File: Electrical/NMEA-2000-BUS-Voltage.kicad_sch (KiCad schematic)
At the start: 68 parts, among them IC1 ADS131M08QPBSRQ1, J1 DE9_Receptacle, J2 Conn_01x04, J3 Conn_01x02, J4 Conn_01x04, J5 Conn_01x05, J6 Conn_01x02, Q1 IRFZ44N, SW1 SW_Push, U1 ESP32-WROOM-32E, U2 LM7805_TO220, U3 AP2112K-3.3, U4 BME280, U5 SN65HVD230, U6 ADR4533, Y1 Crystal

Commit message: Updated Schematics
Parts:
- removed C1, C4, C5: 0.1uF, Capacitor_THT:C_Disc_D3.0mm_W1.6mm_P2.50mm, symbol Device:C_Small
- removed C10: 0.1nF, Connector_PinHeader_2.54mm:PinHeader_1x02_P2.54mm_Vertical, symbol Device:C_Small
- removed C15: 0.1uF, Capacitor_THT:C_Disc_D3.0mm_W1.6mm_P2.50mm, symbol Device:C
- removed C6: 1uF, Capacitor_THT:C_Disc_D3.0mm_W1.6mm_P2.50mm, symbol Device:C_Small
- removed D5, D6: LED, LED_THT:LED_D5.0mm, symbol Device:LED
- removed D7: D_Schottky, Diode_THT:D_DO-201_P15.24mm_Horizontal, symbol Device:D_Schottky
- removed IC1: ADS131M08QPBSRQ1, symbol ADS131M08QPBSRQ1:ADS131M08QPBSRQ1
- removed J1: DE9_Receptacle, symbol Connector:DE9_Receptacle
- removed J3: Conn_01x02, TerminalBlock_Phoenix:TerminalBlock_Phoenix_PT-1,5-2-5.0-H_1x02_P5.00mm_Horizontal, symbol Connector_Generic:Conn_01x02
- removed J5: Conn_01x05, TerminalBlock_Phoenix:TerminalBlock_Phoenix_PT-1,5-5-5.0-H_1x05_P5.00mm_Horizontal, symbol Connector_Generic:Conn_01x05
- removed J6: Conn_01x02, symbol Connector_Generic:Conn_01x02
- removed Q1: IRFZ44N, Package_TO_SOT_THT:TO-220-3_Vertical, symbol Simulation_SPICE:NMOS
- removed R1: R_Small, symbol Device:R_Small
- removed R12, R13: 220R, symbol Device:R
- removed R14, R15: 4.7k, symbol Device:R_Small
- removed R17: 150R, symbol Device:R_Small
- removed R18, R5: 10k, symbol Device:R
- removed R2, R6: 10k, Resistor_THT:R_Axial_DIN0204_L3.6mm_D1.6mm_P5.08mm_Horizontal, symbol Device:R_Small
- removed R20: 10k, Resistor_THT:R_Axial_DIN0204_L3.6mm_D1.6mm_P5.08mm_Horizontal, symbol Device:R
- removed R21: 4k7, Resistor_THT:R_Axial_DIN0204_L3.6mm_D1.6mm_P5.08mm_Horizontal, symbol Device:R
- removed R4: 1k, symbol Device:R
- removed R7: 3.3k, Resistor_THT:R_Axial_DIN0204_L3.6mm_D1.6mm_P5.08mm_Horizontal, symbol Device:R_Small
- removed TH1: NTC, symbol Device:Thermistor_NTC
- removed U1: ESP32-WROOM-32E, RF_Module:ESP32-WROOM-32D, symbol RF_Module:ESP32-WROOM-32E
- removed U3: AP2112K-3.3, Package_TO_SOT_SMD:SOT-23-5, symbol Regulator_Linear:AP2112K-3.3
- removed U4: BME280, Package_LGA:Bosch_LGA-8_2.5x2.5mm_P0.65mm_ClockwisePinNumbering, symbol Sensor:BME280
- removed U6: ADR4533, Package_SO:SOIC-8_3.9x4.9mm_P1.27mm, symbol Reference_Voltage:ADR4533
- removed Y1: Crystal, symbol Device:Crystal
- added C1, C19, C20, C5, C6: 0.1uF, Capacitor_THT:C_Disc_D5.0mm_W2.5mm_P5.00mm, symbol Device:C
- added C10: 1uF, Capacitor_THT:C_Disc_D5.0mm_W2.5mm_P5.00mm, symbol Device:C
- added C12, C15: 20pF, Capacitor_THT:C_Disc_D5.0mm_W2.5mm_P5.00mm, symbol Device:C_Small
- added C17: 0.1uF, Capacitor_THT:C_Disc_D5.0mm_W2.5mm_P5.00mm, symbol Device:C_Small
- added C18: 0.1nF, Capacitor_THT:C_Disc_D5.0mm_W2.5mm_P5.00mm, symbol Device:C_Small
- added C8: 10nF, Capacitor_THT:C_Disc_D5.0mm_W2.5mm_P5.00mm, symbol Device:C
- added D1: 1N5819, Diode_THT:D_DO-41_SOD81_P10.16mm_Horizontal, symbol Device:D_Schottky_Small
- added H1, H2, H3, H4: MountingHole_Pad, MountingHole:MountingHole_6mm_Pad, symbol Mechanical:MountingHole_Pad
- added J2: Conn_01x04, Connector_PinSocket_2.54mm:PinSocket_1x04_P2.54mm_Horizontal, symbol Connector_Generic:Conn_01x04
- added J3: Conn_02x08_Counter_Clockwise, Connector_PinHeader_2.54mm:PinHeader_2x09_P2.54mm_Vertical, symbol Connector_Generic:Conn_02x09_Counter_Clockwise
- added JP1: Jumper_2_Open, Connector_PinHeader_2.54mm:PinHeader_1x02_P2.54mm_Vertical, symbol Jumper:Jumper_2_Open
- added L1: CBG322513U102T, Inductor_SMD:L_1210_3225Metric_Pad1.42x2.65mm_HandSolder, symbol Device:FerriteBead
- added R1: 10k, Resistor_THT:R_Axial_DIN0207_L6.3mm_D2.5mm_P10.16mm_Horizontal, symbol Device:R
- added R10: 10k, Resistor_THT:R_Axial_DIN0207_L6.3mm_D2.5mm_P10.16mm_Horizontal, symbol Device:R_Small
- added R11: 3.3k, Resistor_THT:R_Axial_DIN0207_L6.3mm_D2.5mm_P10.16mm_Horizontal, symbol Device:R_Small
- added R2: 0R, Resistor_THT:R_Axial_DIN0207_L6.3mm_D2.5mm_P10.16mm_Horizontal, symbol Device:R
- added SW2: SW_Push, Button_Switch_THT:SW_PUSH_6mm, symbol Switch:SW_Push
- added U2: AMS1117-3.3, Package_TO_SOT_SMD:SOT-223-3_TabPin2, symbol Regulator_Linear:AMS1117-3.3
- added U3: STM32G431CBTx, Package_QFP:LQFP-48_7x7mm_P0.5mm, symbol MCU_ST_STM32G4:STM32G431CBTx
- added U5: BMP280, N2K-influx:Bosch_LGA-8_2x2.5mm_P0.65mm_ClockwisePinNumbering, symbol Sensor_Pressure:BMP280
- added Y1: K7A080002020, Crystal:Crystal_SMD_7050-4Pin_7.0x5.0mm, symbol Device:Crystal_GND24
- added Y2: X308032768KGB2SC, Crystal:Crystal_C38-LF_D3.0mm_L8.0mm_Horizontal, symbol Device:Crystal
- C11, C14, C9: footprint Capacitor_THT:C_Disc_D3.0mm_W1.6mm_P2.50mm -> Capacitor_THT:C_Disc_D5.0mm_W2.5mm_P5.00mm
- C13: value 220nF -> 0.1uF; footprint Capacitor_THT:C_Disc_D3.0mm_W1.6mm_P2.50mm -> Capacitor_THT:C_Disc_D5.0mm_W2.5mm_P5.00mm
- C16: renamed from C12; footprint Capacitor_THT:C_Disc_D3.0mm_W1.6mm_P2.50mm -> Capacitor_THT:C_Disc_D5.0mm_W2.5mm_P5.00mm
- C2: value 22uF -> 0.1uF; footprint Capacitor_THT:C_Disc_D3.0mm_W1.6mm_P2.50mm -> Capacitor_THT:C_Disc_D5.0mm_W2.5mm_P5.00mm
- C3, C7: value 0.1uF -> 20pF; footprint Capacitor_THT:C_Disc_D3.0mm_W1.6mm_P2.50mm -> Capacitor_THT:C_Disc_D5.0mm_W2.5mm_P5.00mm
- C4: renamed from C8; footprint Capacitor_THT:C_Disc_D3.0mm_W1.6mm_P2.50mm -> Capacitor_THT:C_Disc_D5.0mm_W2.5mm_P5.00mm
- F1: footprint Diode_THT:D_DO-247_Horizontal_TabDown -> Diode_SMD:D_1210_3225Metric_Pad1.42x2.65mm_HandSolder
- JP2: renamed from JP1; footprint Connector_PinSocket_2.54mm:PinSocket_1x03_P2.54mm_Vertical -> Connector_PinHeader_2.54mm:PinHeader_1x03_P2.54mm_Vertical
- JP3: renamed from JP2; footprint Connector_PinSocket_2.54mm:PinSocket_1x03_P2.54mm_Vertical -> Connector_PinHeader_2.54mm:PinHeader_1x03_P2.54mm_Vertical
- R3: value 1k -> 10k; footprint (none) -> Resistor_THT:R_Axial_DIN0207_L6.3mm_D2.5mm_P10.16mm_Horizontal
- R4: renamed from R8; value 680R -> 1.2k; footprint Resistor_THT:R_Axial_DIN0204_L3.6mm_D1.6mm_P5.08mm_Horizontal -> Resistor_THT:R_Axial_DIN0207_L6.3mm_D2.5mm_P10.16mm_Horizontal
- R5: renamed from R9; value 270R -> 470R; footprint Resistor_THT:R_Axial_DIN0204_L3.6mm_D1.6mm_P5.08mm_Horizontal -> Resistor_THT:R_Axial_DIN0207_L6.3mm_D2.5mm_P10.16mm_Horizontal
- R6: renamed from R16; footprint (none) -> Resistor_THT:R_Axial_DIN0207_L6.3mm_D2.5mm_P10.16mm_Horizontal
- R7: renamed from R10; value 220R -> 330R; footprint Resistor_THT:R_Axial_DIN0204_L3.6mm_D1.6mm_P5.08mm_Horizontal -> Resistor_THT:R_Axial_DIN0207_L6.3mm_D2.5mm_P10.16mm_Horizontal
- R8: renamed from R11; value 820R -> 1k5; footprint Resistor_THT:R_Axial_DIN0204_L3.6mm_D1.6mm_P5.08mm_Horizontal -> Resistor_THT:R_Axial_DIN0207_L6.3mm_D2.5mm_P10.16mm_Horizontal
- R9: renamed from R19; footprint Resistor_THT:R_Axial_DIN0204_L3.6mm_D1.6mm_P5.08mm_Horizontal -> Resistor_THT:R_Axial_DIN0207_L6.3mm_D2.5mm_P10.16mm_Horizontal
- SW1: footprint (none) -> Button_Switch_THT:SW_PUSH_6mm
- TP1, TP2, TP3, TP4: footprint (none) -> TestPoint:TestPoint_Pad_3.0x3.0mm
- renumbered D1 to D2, D2 to D3, D3 to D4, D4 to D5, J2 to J1, JP3 to JP4, U2 to U1, U5 to U4
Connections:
- net AIN1P is gone; now on net +3.3V: R3.2
- net +12V: now also JP1.2 (B)
- net +3.3V: now also C16.1, R7.1, SW1.1, TP3.1, C1.1, C19.1, C20.1, C5.1, C6.1, D1.2 (A), L1.1, R10.1, U2.2 (VO), U3.24 (VDD), U3.36 (VDD), U3.48 (VDD), U5.2 (CSB), U5.6 (VDDIO), U5.8 (VDD); no longer C7.1
- net +5V: now also J2.1 (Pin_1), U2.3 (VI)
- net GND: now also C14.1, C3.2, C1.2, C10.2, C12.2, C15.2, C17.2, C18.2, C19.2, C20.2, C6.2, C8.2, H1.1, H2.1, H3.1, H4.1, J2.4 (Pin_4), R1.1, SW2.1, U2.1 (GND), U3.19 (VSSA), U3.23 (VSS), U3.35 (VSS), U3.47 (VSS), U5.1 (GND), U5.5 (SDO), U5.7 (GND), Y1.2, Y1.4; no longer C14.2
- net MISO: now also U3.14 (PA6)
- net MOSI: now also U3.15 (PA7)
- net PWM: now also U3.38 (PA14)
- net RX: now also J2.2 (Pin_2), U3.32 (PA10)
- net SCL: now also U3.30 (PA8), U5.4 (SCK)
- net SCLK: now also U3.13 (PA5)
- net SDA: now also U5.3 (SDI)
- net TACHO: now also R11.2
- net TX: now also J2.3 (Pin_3), U3.31 (PA9)
- net VMot: now also JP1.1 (A)
- net ~{CS}: now also U3.12 (PA4)
- net ~{DRDY}: now also U3.37 (PA13)
- net at SW1.2: now also C5.2, R1.2, U3.45 (PB8); no longer C3.2
- net V_{ref}+: now reaches C13.1
- net V_{ref}+: now also R2.2, U3.20 (VREF+)
- net at C3.1: now also U3.6 (PF1), Y1.1; no longer SW1.1
- removed net +3V3: C14.1, C16.1, R7.1, TP3.1
- net CAN_RX renamed CAN_{RX}
- net CAN_{RX}: now also U3.34 (PA12)
- net CAN_TX renamed CAN_{TX}
- net CAN_{TX}: now also U3.33 (PA11)
- net V_{ref} renamed EN
- net EN: now also C14.2, SW2.2, U3.7 (PG10)
- new net: C17.1, D1.1 (K), U3.1 (VBAT)
- new net: C7.1, U3.5 (PF0), Y1.3
- new net: C12.1, U3.4 (PC15), Y2.1
- new net: C15.1, U3.3 (PC14), Y2.2
- new net +3.3VA: C10.1, C8.1, L1.2, R2.1, U3.21 (VDDA)
- new net PA15: C18.1, R10.2, R11.1, U3.39 (PA15)
- new net PA2: J3.1 (Pin_1), U3.10 (PA2)
- new net PA3: J3.2 (Pin_2), U3.11 (PA3)
- new net PB0: J3.3 (Pin_3), U3.16 (PB0)
- new net PB1: J3.4 (Pin_4), U3.17 (PB1)
- new net PB10: J3.16 (Pin_16), U3.22 (PB10)
- new net PB11: J3.15 (Pin_15), U3.25 (PB11)
- new net PB12: J3.14 (Pin_14), U3.26 (PB12)
- new net PB13: J3.13 (Pin_13), U3.27 (PB13)
- new net PB14: J3.12 (Pin_12), U3.28 (PB14)
- new net PB15: J3.11 (Pin_11), U3.29 (PB15)
- new net PB2: J3.5 (Pin_5), U3.18 (PB2)
- new net PB3: J3.6 (Pin_6), U3.40 (PB3)
- new net PB4: J3.7 (Pin_7), U3.41 (PB4)
- new net PB5: J3.8 (Pin_8), U3.42 (PB5)
- new net PB6: J3.9 (Pin_9), U3.43 (PB6)
- new net PB7: J3.18 (Pin_18), U3.44 (PB7)
- new net PB9: J3.17 (Pin_17), U3.46 (PB9)
- new net PC13: J3.10 (Pin_10), U3.2 (PC13)
- new net REL1: U3.8 (PA0)
- new net REL2: U3.9 (PA1)
- no-connect marks 28 -> 1
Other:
- added sheet Sensor (sensor.kicad_sch)
- note added: "Boot Switch"
- note added: "CAN-Transceiver"
- note added: "External Connectors"
- note added: "Mounting & Testing"
- note added: "Power Supply"
- note added: "STM32G431 & Peripherals"
- note added: "Temp-Sensor"
- moved on the sheet: C11, C16, C4, C9, D2, D3, D4, D5, F1, J1, J4, JP2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

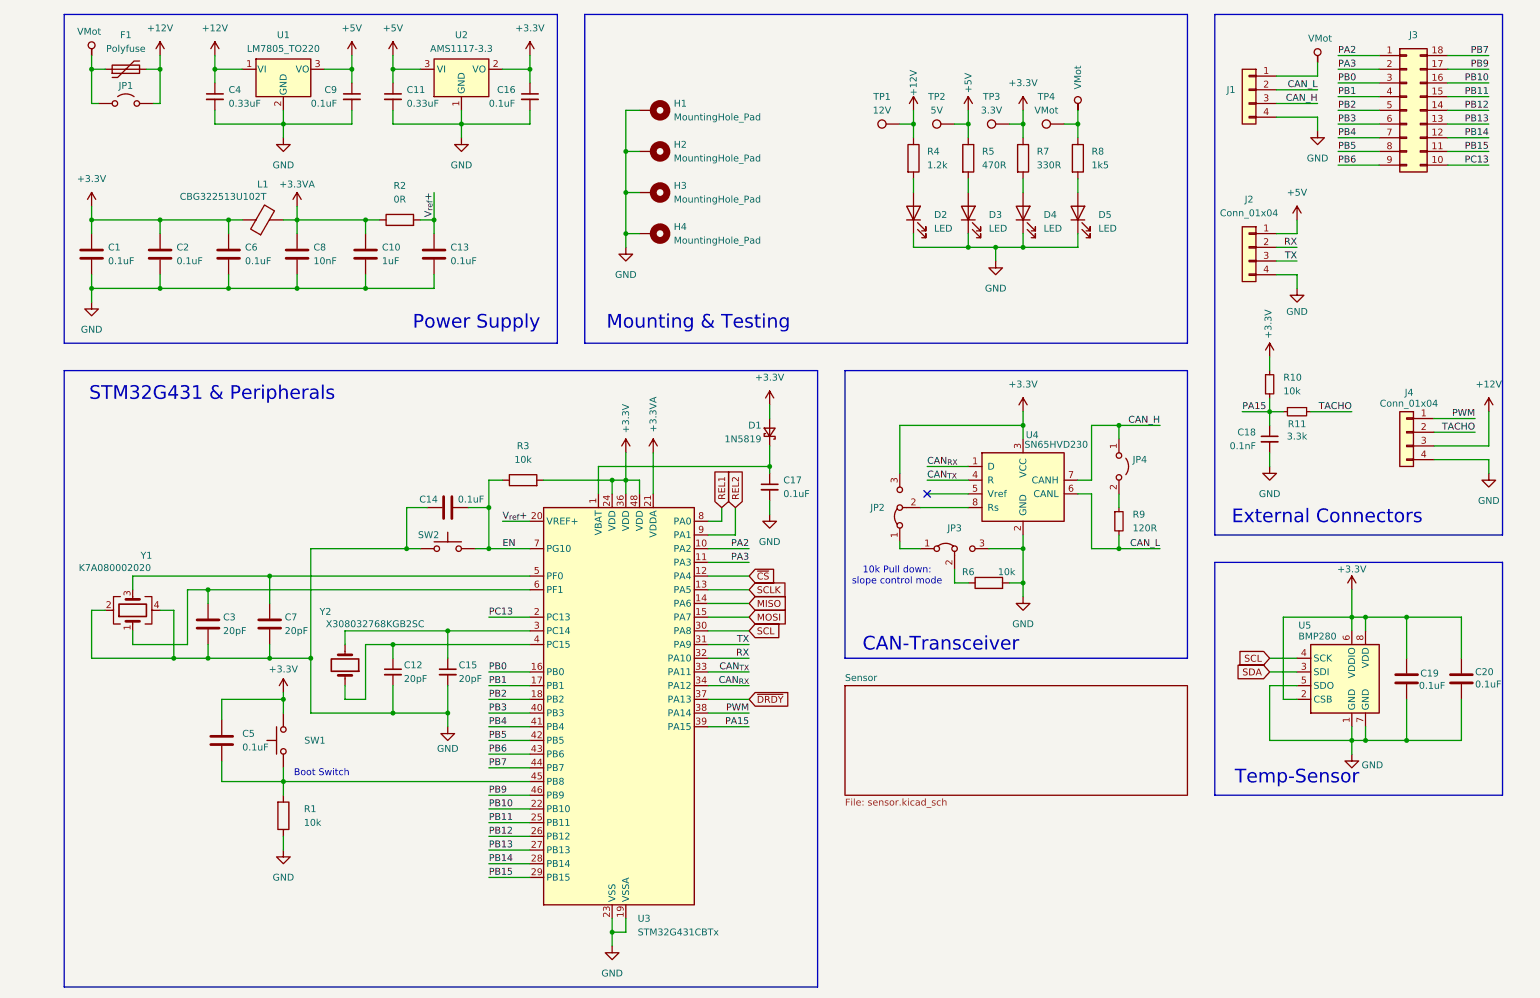
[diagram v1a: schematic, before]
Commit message: Replaced SN65HVD230 with MCP2562
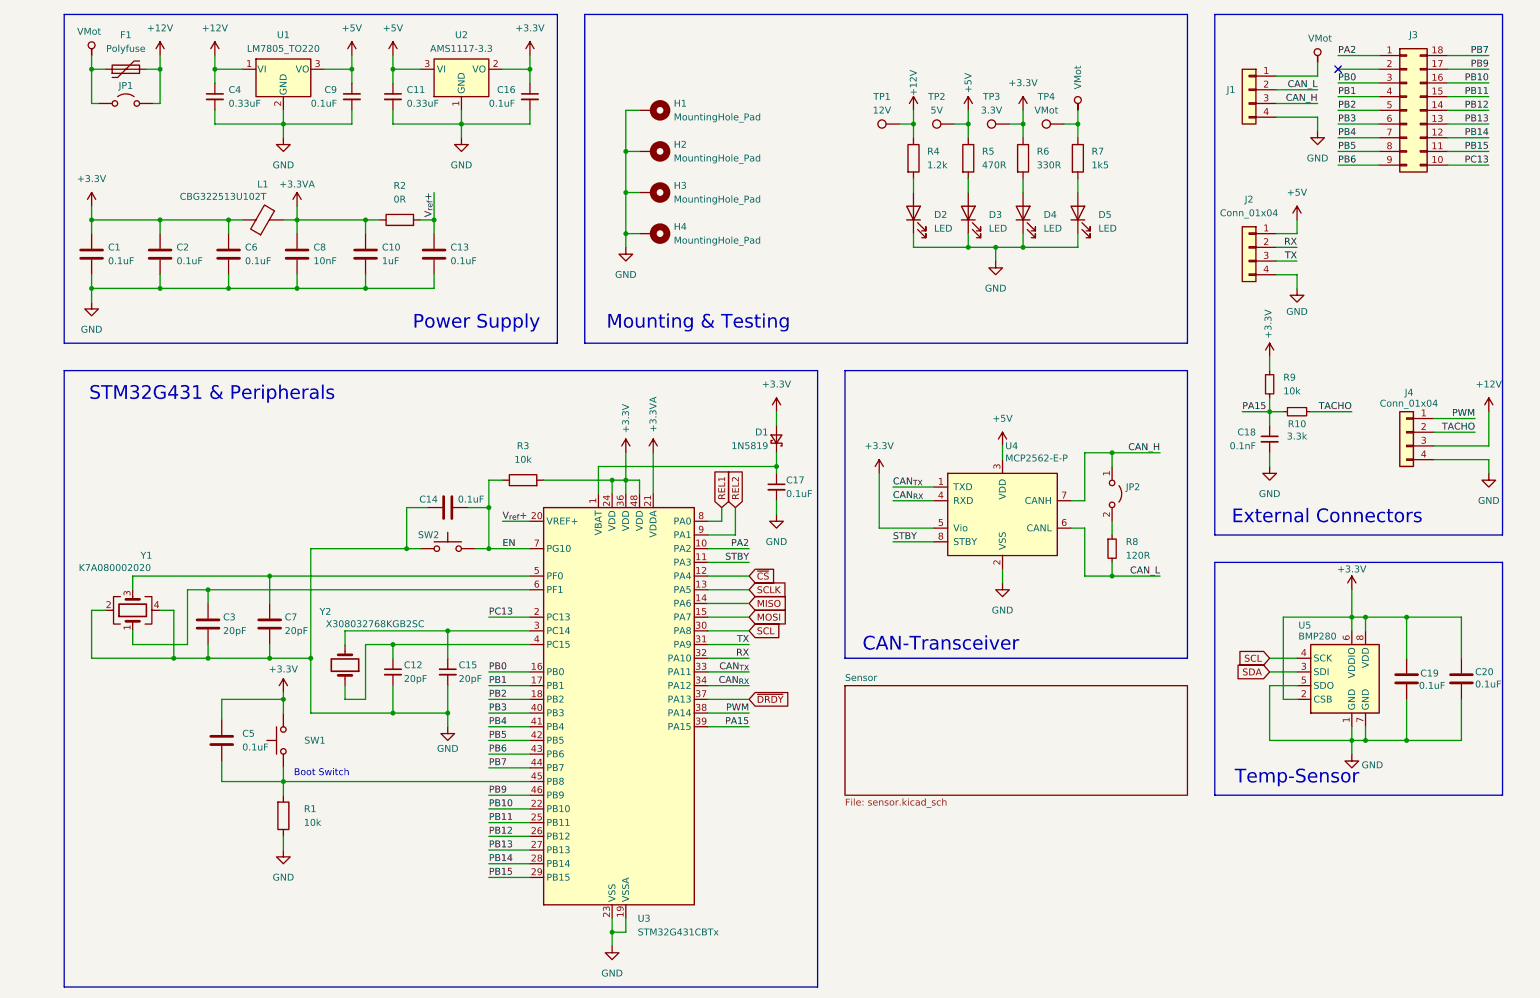
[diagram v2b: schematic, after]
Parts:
- removed JP2, JP3: Jumper_3_Bridged12, Connector_PinHeader_2.54mm:PinHeader_1x03_P2.54mm_Vertical, symbol Jumper:Jumper_3_Bridged12
- removed JP4: Jumper_2_Open, Connector_PinHeader_2.54mm:PinHeader_1x02_P2.54mm_Vertical, symbol Jumper:Jumper_2_Open
- removed R6: 10k, Resistor_THT:R_Axial_DIN0207_L6.3mm_D2.5mm_P10.16mm_Horizontal, symbol Device:R
- removed R9: 120R, Resistor_THT:R_Axial_DIN0207_L6.3mm_D2.5mm_P10.16mm_Horizontal, symbol Device:R_Small
- removed U4: SN65HVD230, Package_SO:SOIC-8_3.9x4.9mm_P1.27mm, symbol Interface_CAN_LIN:SN65HVD230
- added JP2: Jumper_2_Open, Connector_PinHeader_2.54mm:PinHeader_1x02_P2.54mm_Vertical, symbol Jumper:Jumper_2_Open
- added R8: 120R, Resistor_THT:R_Axial_DIN0207_L6.3mm_D2.5mm_P10.16mm_Horizontal, symbol Device:R_Small
- added U4: MCP2562-E-P, Package_DIP:DIP-8_W7.62mm, symbol Interface_CAN_LIN:MCP2562-E-P
- renumbered R11 to R10, R7 to R6, R8 to R7, R10 to R9
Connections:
- net +3.3V: now also U4.5 (Vio)
- net +5V: now also U4.3 (VDD)
- net CAN_H: now also JP2.1 (A), U4.7 (CANH)
- net CAN_L: now also R8.2, U4.6 (CANL)
- net CAN_{RX}: now also U4.4 (RXD)
- net CAN_{TX}: now also U4.1 (TXD)
- net GND: now also U4.2 (VSS)
- net PA3: no longer names the net of J3.2 (Pin_2)
- net PA3: no longer U3.11 (PA3)
- new net: JP2.2 (B), R8.1
- new net STBY: U3.11 (PA3), U4.8 (STBY)
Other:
- note removed: "10k Pull down: slope control mode"
- moved on the sheet: C17, D1

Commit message: Cleaned Up Project Updated BOM Updated Naming
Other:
- sheet Sensor: file sensor.kicad_sch -> NMEA-2000-Bus-Voltage-sensor.kicad_sch
- title: Bus Power -> N2k Bus Power
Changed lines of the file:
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@@
 	(paper "A4")
 	(title_block
-		(title "Bus Power")
-		(date "2024-06-12")
-		(rev "2")
+		(title "N2k Bus Power")
+		(date "2024-07-06")
+		(rev "3")
 		(company "Johannes Höllwerth")
+		(comment 1 "Main Systems")
 	)
 	(junction
@@
 			)
 		)
-		(property "Sheetfile" "sensor.kicad_sch"
+		(property "Sheetfile" "NMEA-2000-Bus-Voltage-sensor.kicad_sch"
 			(at 160.02 160.6046 0)
 			(effects
